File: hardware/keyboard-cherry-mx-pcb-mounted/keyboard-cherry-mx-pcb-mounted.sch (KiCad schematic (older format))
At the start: 1 part

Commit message: Adds general layout for the custom keyboard.
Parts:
- gave numbers to parts that had none: 1
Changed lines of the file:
@@
 $EndSheet
 $Comp
-L Sij_MCU:BGM13S U?
+L Sij_MCU:BGM13S U1
 U 1 1 5E85FADA
 P 6000 4000
-F 0 "U?" H 6000 4100 50  0000 C CNN
+F 0 "U1" H 6000 4100 50  0000 C CNN
 F 1 "BGM13S" H 6000 4000 50  0000 C CNN
 F 2 "Sij_MCU:BGM13S" H 6000 4150 50  0001 C CNN
@@
 	5600 5500 5700 5500
 $Comp
-L power:GND #PWR?
+L power:GND #PWR0101
 U 1 1 5E864ACF
 P 6000 5600
-F 0 "#PWR?" H 6000 5350 50  0001 C CNN
+F 0 "#PWR0101" H 6000 5350 50  0001 C CNN
 F 1 "GND" H 6005 5427 50  0000 C CNN
 F 2 "" H 6000 5600 50  0001 C CNN
@@
 SWO
 $Comp
-L power:GND #PWR?
+L power:GND #PWR0102
 U 1 1 5E873C21
 P 4650 3000
-F 0 "#PWR?" H 4650 2750 50  0001 C CNN
+F 0 "#PWR0102" H 4650 2750 50  0001 C CNN
 F 1 "GND" V 4655 2872 50  0000 R CNN
 F 2 "" H 4650 3000 50  0001 C CNN
@@
 	5100 2800 5200 2800
 $Comp
-L power:+3.3V #PWR?
+L power:+3.3V #PWR0103
 U 1 1 5E87759E
 P 6000 2200
-F 0 "#PWR?" H 6000 2050 50  0001 C CNN
+F 0 "#PWR0103" H 6000 2050 50  0001 C CNN
 F 1 "+3.3V" H 6015 2373 50  0000 C CNN
 F 2 "" H 6000 2200 50  0001 C CNN

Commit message: Adds STM32F413 to cherry mx pcb mounted board.
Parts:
- removed U1: BGM13S, Sij_MCU:BGM13S, symbol Sij_MCU:BGM13S
- added C? (x2): 4.7u, Capacitor_SMD:C_0805_2012Metric, symbol Device:C_Small
- added C? (x2): 15pF, Capacitor_SMD:C_0805_2012Metric, symbol Device:C_Small
- added C? (x4): 0.1u, Capacitor_SMD:C_0805_2012Metric, symbol Device:C_Small
- added C?: 1u, Capacitor_SMD:C_0805_2012Metric, symbol Device:C_Small
- added JP?: BootJumper, Jumper:SolderJumper-3_P1.3mm_Bridged12_Pad1.0x1.5mm, symbol Jumper:SolderJumper_3_Bridged12
- added SW?: RST, Button_Switch_SMD:SW_SPST_B3U-1000P, symbol Switch:SW_Push
- added U?: STM32F413CHUx, Package_DFN_QFN:QFN-48-1EP_7x7mm_P0.5mm_EP5.6x5.6mm, symbol MCU_ST_STM32F4:STM32F413CHUx
- added Y?: 8MHz, Crystal:Crystal_SMD_TXC_7A-2Pin_5x3.2mm, symbol Device:Crystal_Small
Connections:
- net labels added: D+, D-, OSC_IN, OSC_OUT, VBUS_SENSE, VCAP, ~NRST
- net labels removed: C15, SWO
- wire segments 56 -> 93
- no-connect marks 1 -> 0
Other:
- note added: "Reset Button"
- note added: "VDD Bypass Capacitors"
- note added: "VDDA Bypass Capacitors"

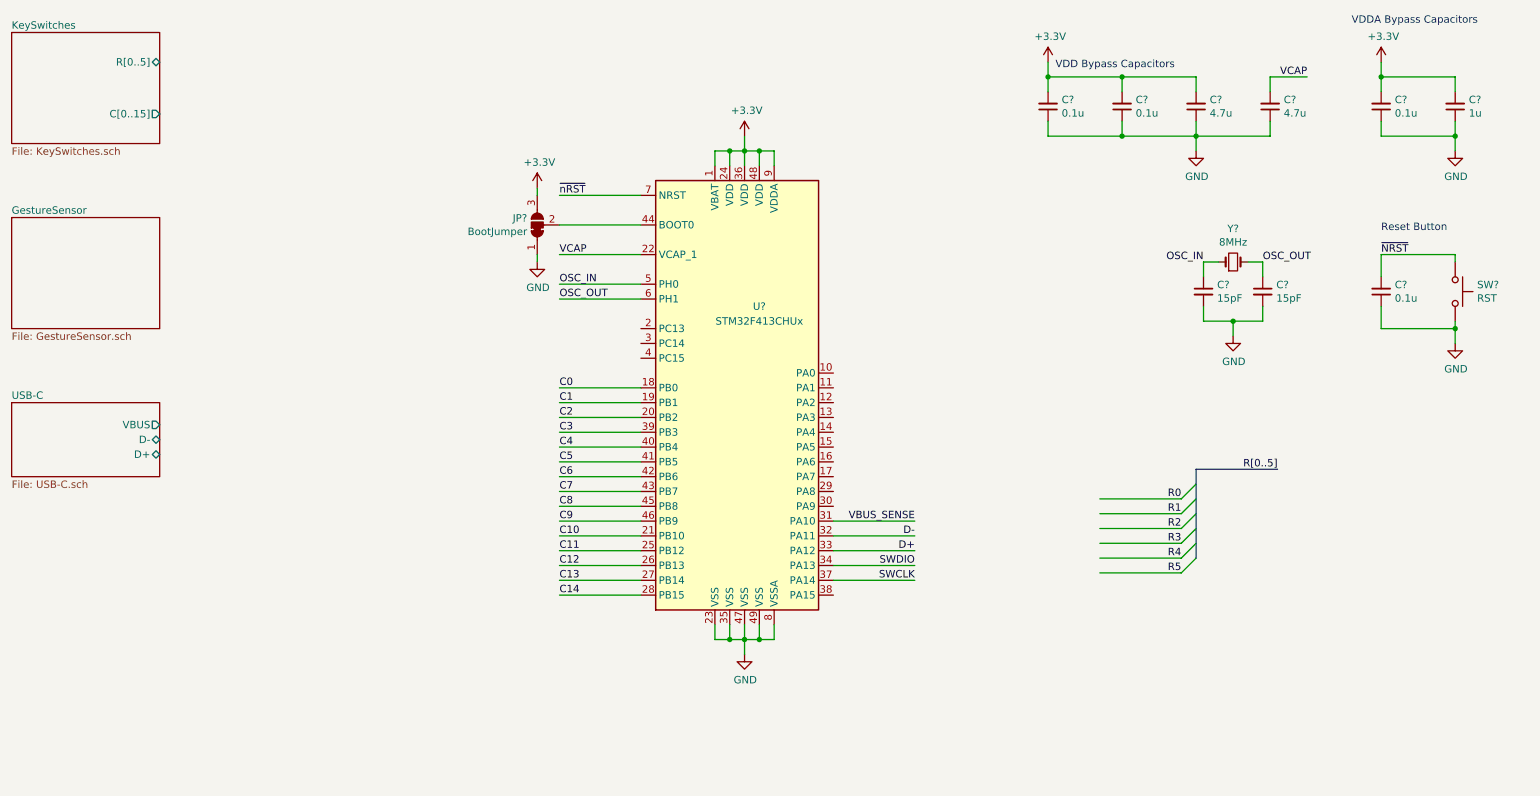
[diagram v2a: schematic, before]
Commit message: Adds gesture sensor interface. May change to bigger stm32 package.
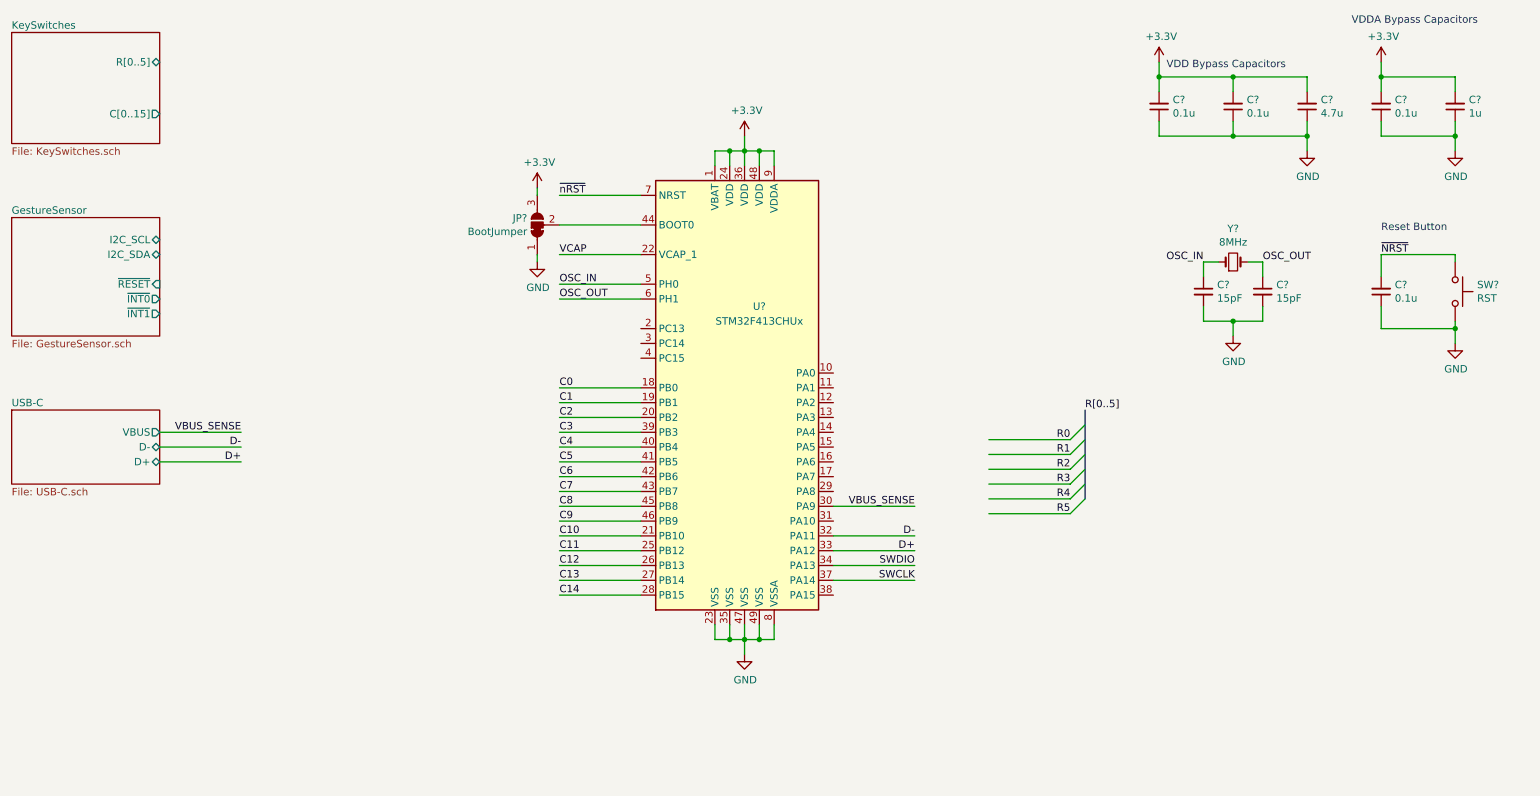
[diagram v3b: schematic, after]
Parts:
- removed C?: 4.7u, Capacitor_SMD:C_0805_2012Metric, symbol Device:C_Small
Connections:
- wire segments 93 -> 92
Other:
- moved on the sheet: C?
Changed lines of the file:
@@
 $EndComp
 $Sheet
-S 1000 2250 1000 750
+S 1000 2250 1000 800
 U 5E8711BD
 F0 "GestureSensor" 50
 F1 "GestureSensor.sch" 50
+F2 "I2C_SCL" B R 2000 2400 50
+F3 "I2C_SDA" B R 2000 2500 50
+F4 "~RESET" I R 2000 2700 50
+F5 "~INT0" O R 2000 2800 50
+F6 "~INT1" O R 2000 2900 50
 $EndSheet
 Wire Wire Line
@@
 ~nRST
 Wire Wire Line
-	8350 4150 8900 4150
-Wire Wire Line
-	8900 4250 8350 4250
-Wire Wire Line
-	8350 4350 8900 4350
-Wire Wire Line
-	8350 4450 8900 4450
-Text Label 8900 4150 2    50   ~ 0
+	7600 3750 8150 3750
+Wire Wire Line
+	8150 3850 7600 3850
+Wire Wire Line
+	7600 3950 8150 3950
+Wire Wire Line
+	7600 4050 8150 4050
+Text Label 8150 3750 2    50   ~ 0
 R0
-Text Label 8900 4250 2    50   ~ 0
+Text Label 8150 3850 2    50   ~ 0
 R1
-Text Label 8900 4350 2    50   ~ 0
+Text Label 8150 3950 2    50   ~ 0
 R2
-Text Label 8900 4450 2    50   ~ 0
+Text Label 8150 4050 2    50   ~ 0
 R3
 Wire Wire Line
-	8350 4550 8900 4550
-Wire Wire Line
-	8900 4650 8350 4650
-Text Label 8900 4550 2    50   ~ 0
+	7600 4150 8150 4150
+Wire Wire Line
+	8150 4250 7600 4250
+Text Label 8150 4150 2    50   ~ 0
 R4
-Text Label 8900 4650 2    50   ~ 0
+Text Label 8150 4250 2    50   ~ 0
 R5
 Entry Wire Line
-	9000 4550 8900 4650
+	8250 4150 8150 4250
 Entry Wire Line
-	9000 4450 8900 4550
+	8250 4050 8150 4150
 Entry Wire Line
-	9000 4350 8900 4450
+	8250 3950 8150 4050
 Entry Wire Line
-	9000 4250 8900 4350
+	8250 3850 8150 3950
 Entry Wire Line
-	9000 4150 8900 4250
+	8250 3750 8150 3850
 Entry Wire Line
-	9000 4050 8900 4150
-Wire Bus Line
-	9000 3950 9550 3950
-Text Label 9550 3950 2    50   ~ 0
+	8250 3650 8150 3750
+Text Label 8250 3550 0    50   ~ 0
 R[0..5]
 Wire Wire Line
@@
 	5850 1800 5950 1800
 $Comp
-L Device:C_Small C?
-U 1 1 5E71757F
-P 9500 1500
-F 0 "C?" H 9408 1454 50  0000 R CNN
-F 1 "4.7u" H 9408 1545 50  0000 R CNN
-F 2 "Capacitor_SMD:C_0805_2012Metric" H 9500 1500 50  0001 C CNN
-F 3 "~" H 9500 1500 50  0001 C CNN
-	1    9500 1500
-	-1   0    0    1
-$EndComp
-$Comp
 L Jumper:SolderJumper_3_Bridged12 JP?
 U 1 1 5E719EA9
@@
 L Device:C_Small C?
 U 1 1 5E73F523
-P 8000 1500
-F 0 "C?" H 7908 1454 50  0000 R CNN
-F 1 "0.1u" H 7908 1545 50  0000 R CNN
-F 2 "Capacitor_SMD:C_0805_2012Metric" H 8000 1500 50  0001 C CNN
-F 3 "~" H 8000 1500 50  0001 C CNN
-	1    8000 1500
+P 8750 1500
+F 0 "C?" H 8658 1454 50  0000 R CNN
+F 1 "0.1u" H 8658 1545 50  0000 R CNN
+F 2 "Capacitor_SMD:C_0805_2012Metric" H 8750 1500 50  0001 C CNN
+F 3 "~" H 8750 1500 50  0001 C CNN
+	1    8750 1500
 	-1   0    0    1
 $EndComp
@@
 L Device:C_Small C?
 U 1 1 5E73FD52
-P 8500 1500
-F 0 "C?" H 8408 1454 50  0000 R CNN
-F 1 "0.1u" H 8408 1545 50  0000 R CNN
-F 2 "Capacitor_SMD:C_0805_2012Metric" H 8500 1500 50  0001 C CNN
-F 3 "~" H 8500 1500 50  0001 C CNN
-	1    8500 1500
+P 9250 1500
+F 0 "C?" H 9158 1454 50  0000 R CNN
+F 1 "0.1u" H 9158 1545 50  0000 R CNN
+F 2 "Capacitor_SMD:C_0805_2012Metric" H 9250 1500 50  0001 C CNN
+F 3 "~" H 9250 1500 50  0001 C CNN
+	1    9250 1500
 	-1   0    0    1
 $EndComp
@@
 L Device:C_Small C?
 U 1 1 5E73FF6A
-P 9000 1500
-F 0 "C?" H 8908 1454 50  0000 R CNN
-F 1 "4.7u" H 8908 1545 50  0000 R CNN
-F 2 "Capacitor_SMD:C_0805_2012Metric" H 9000 1500 50  0001 C CNN
-F 3 "~" H 9000 1500 50  0001 C CNN
-	1    9000 1500
+P 9750 1500
+F 0 "C?" H 9658 1454 50  0000 R CNN
+F 1 "4.7u" H 9658 1545 50  0000 R CNN
+F 2 "Capacitor_SMD:C_0805_2012Metric" H 9750 1500 50  0001 C CNN
+F 3 "~" H 9750 1500 50  0001 C CNN
+	1    9750 1500
 	-1   0    0    1
 $EndComp
@@
 L power:+3.3V #PWR?
 U 1 1 5E743BF3
-P 8000 1200
-F 0 "#PWR?" H 8000 1050 50  0001 C CNN
-F 1 "+3.3V" H 8015 1373 50  0000 C CNN
-F 2 "" H 8000 1200 50  0001 C CNN
-F 3 "" H 8000 1200 50  0001 C CNN
-	1    8000 1200
-	1    0    0    -1
-$EndComp
-Wire Wire Line
-	9000 1300 9000 1400
-Wire Wire Line
-	8500 1400 8500 1300
-Connection ~ 8500 1300
-Wire Wire Line
-	8500 1300 9000 1300
-Wire Wire Line
-	8000 1400 8000 1300
-Wire Wire Line
-	8000 1300 8500 1300
+P 8750 1200
+F 0 "#PWR?" H 8750 1050 50  0001 C CNN
+F 1 "+3.3V" H 8765 1373 50  0000 C CNN
+F 2 "" H 8750 1200 50  0001 C CNN
+F 3 "" H 8750 1200 50  0001 C CNN
+	1    8750 1200
+	1    0    0    -1
+$EndComp
+Wire Wire Line
+	9750 1300 9750 1400
+Wire Wire Line
+	9250 1400 9250 1300
+Connection ~ 9250 1300
+Wire Wire Line
+	9250 1300 9750 1300
+Wire Wire Line
+	8750 1400 8750 1300
+Wire Wire Line
+	8750 1300 9250 1300
 $Comp
 L power:GND #PWR?
 U 1 1 5E748424
-P 9000 1800
-F 0 "#PWR?" H 9000 1550 50  0001 C CNN
-F 1 "GND" H 9005 1627 50  0000 C CNN
-F 2 "" H 9000 1800 50  0001 C CNN
-F 3 "" H 9000 1800 50  0001 C CNN
-	1    9000 1800
-	1    0    0    -1
-$EndComp
-Wire Wire Line
-	9000 1800 9000 1700
-Wire Wire Line
-	9000 1700 8500 1700
-Connection ~ 9000 1700
-Wire Wire Line
-	9000 1700 9000 1600
-Wire Wire Line
-	8000 1600 8000 1700
-Wire Wire Line
-	8500 1600 8500 1700
-Connection ~ 8500 1700
-Wire Wire Line
-	8500 1700 8000 1700
-Wire Wire Line
-	9500 1400 9500 1300
-Wire Wire Line
-	9500 1300 9750 1300
-Wire Wire Line
-	9500 1700 9500 1600
-Wire Wire Line
-	9500 1700 9000 1700
-Text Label 9750 1300 2    50   ~ 0
-VCAP
+P 9750 1800
+F 0 "#PWR?" H 9750 1550 50  0001 C CNN
+F 1 "GND" H 9755 1627 50  0000 C CNN
+F 2 "" H 9750 1800 50  0001 C CNN
+F 3 "" H 9750 1800 50  0001 C CNN
+	1    9750 1800
+	1    0    0    -1
+$EndComp
+Wire Wire Line
+	9750 1800 9750 1700
+Wire Wire Line
+	9750 1700 9250 1700
+Connection ~ 9750 1700
+Wire Wire Line
+	9750 1700 9750 1600
+Wire Wire Line
+	8750 1600 8750 1700
+Wire Wire Line
+	9250 1600 9250 1700
+Connection ~ 9250 1700
+Wire Wire Line
+	9250 1700 8750 1700
 $Comp
 L Device:C_Small C?
@@
 Text Notes 10050 950  0    50   ~ 0
 VDDA Bypass Capacitors
-Text Notes 8050 1250 0    50   ~ 0
+Text Notes 8800 1250 0    50   ~ 0
 VDD Bypass Capacitors
 $Comp
@@
 OSC_OUT
 $Sheet
-S 1000 3500 1000 500
+S 1000 3550 1000 500
 U 5E7D269A
 F0 "USB-C" 50
 F1 "USB-C.sch" 50
-F2 "D-" B R 2000 3750 50
-F3 "D+" B R 2000 3850 50
-F4 "VBUS" O R 2000 3650 50
+F2 "D-" B R 2000 3800 50
+F3 "D+" B R 2000 3900 50
+F4 "VBUS" O R 2000 3700 50
 $EndSheet
 Wire Wire Line
-	8000 1200 8000 1300
-Connection ~ 8000 1300
+	8750 1200 8750 1300
+Connection ~ 8750 1300
 Wire Wire Line
 	6550 4500 7100 4500
@@
 D+
 Wire Wire Line
-	6550 4300 7100 4300
+	6550 4200 7100 4200
+Text Label 7100 4200 2    50   ~ 0
+VBUS_SENSE
+Wire Wire Line
+	2000 3900 2550 3900
+Wire Wire Line
+	2000 3800 2550 3800
+Text Label 2550 3800 2    50   ~ 0
+D-
+Text Label 2550 3900 2    50   ~ 0
+D+
+Wire Wire Line
+	2000 3700 2550 3700
+Text Label 2550 3700 2    50   ~ 0
+VBUS_SENSE
 Wire Bus Line
-	9000 3950 9000 4550
-Text Label 7100 4300 2    50   ~ 0
-VBUS_SENSE
+	8250 3550 8250 4150
 $EndSCHEMATC

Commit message: Adds completed sensor and power connections. Still need to add USB footprint then sch are done for version 1.0
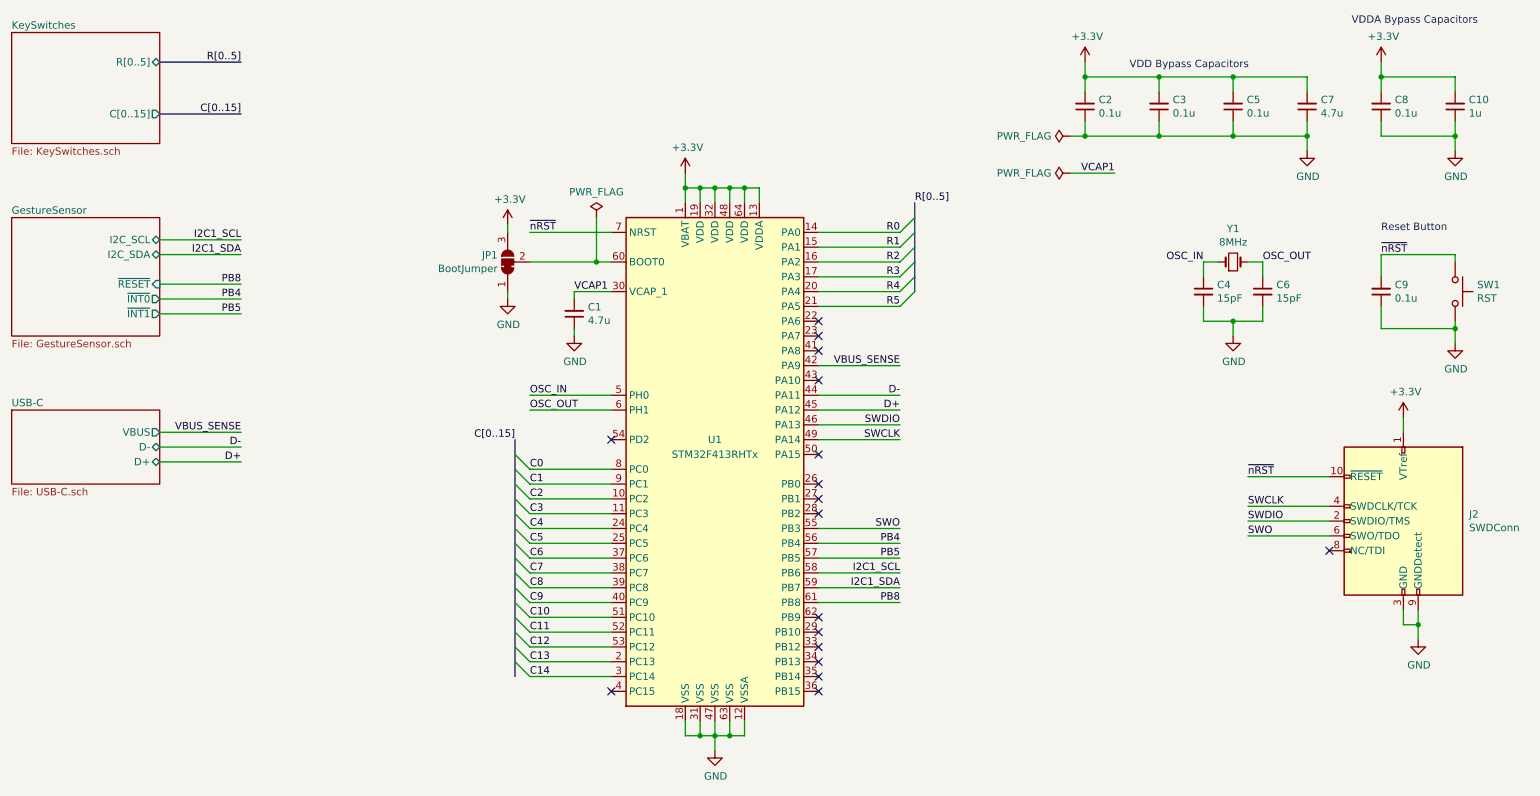
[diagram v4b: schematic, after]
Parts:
- removed JP?: BootJumper, Jumper:SolderJumper-3_P1.3mm_Bridged12_Pad1.0x1.5mm, symbol Jumper:SolderJumper_3_Bridged12
- removed U?: STM32F413CHUx, Package_DFN_QFN:QFN-48-1EP_7x7mm_P0.5mm_EP5.6x5.6mm, symbol MCU_ST_STM32F4:STM32F413CHUx
- added C1: 4.7u, Capacitor_SMD:C_0805_2012Metric, symbol Device:C_Small
- added C2: 0.1u, Capacitor_SMD:C_0805_2012Metric, symbol Device:C_Small
- added J2: SWDConn, Connector:Tag-Connect_TC2050-IDC-NL_2x05_P1.27mm_Vertical, symbol Connector:Conn_ARM_JTAG_SWD_10
- added JP1: BootJumper, Jumper:SolderJumper-3_P1.3mm_Bridged12_Pad1.0x1.5mm, symbol Jumper:SolderJumper_3_Bridged12
- added U1: STM32F413RHTx, Package_QFP:LQFP-64_10x10mm_P0.5mm, symbol MCU_ST_STM32F4:STM32F413RHTx
- gave numbers to parts that had none: 10
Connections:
- net labels added: C[0..15], I2C1_SCL, I2C1_SDA, PB4, PB5, PB8, SWO, VCAP1
- net labels removed: VCAP, ~NRST
- wire segments 92 -> 124
- no-connect marks 0 -> 17

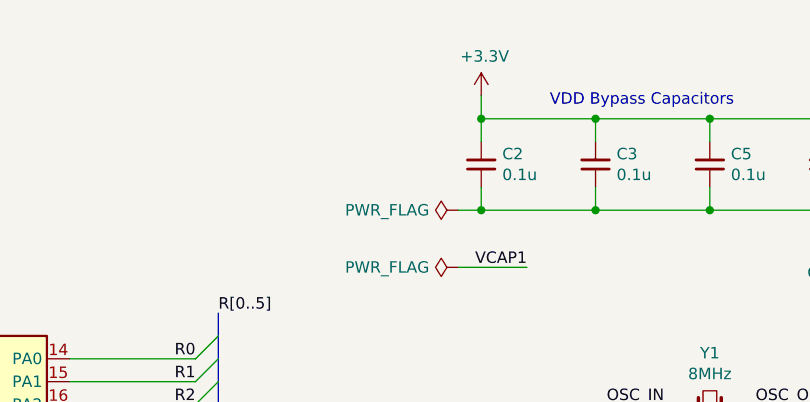
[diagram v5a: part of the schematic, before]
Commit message: Adds final key caps layout of a 75 keyboard.
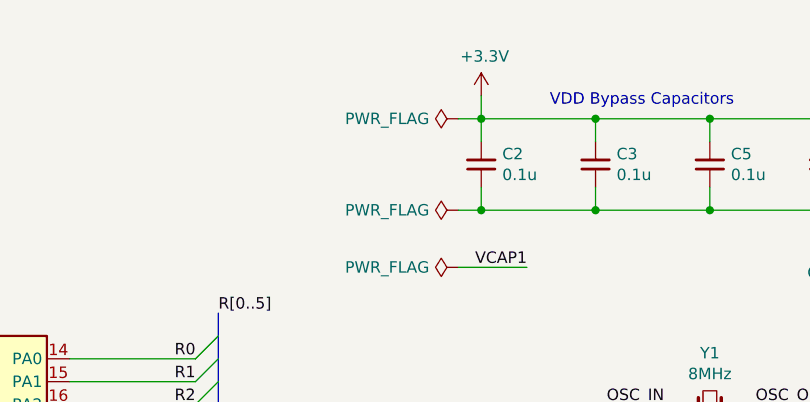
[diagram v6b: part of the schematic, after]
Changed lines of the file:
@@
 Wire Wire Line
 	4950 2550 4500 2550
+$Comp
+L power:PWR_FLAG #FLG0104
+U 1 1 5E7192AF
+P 8150 1300
+F 0 "#FLG0104" H 8150 1375 50  0001 C CNN
+F 1 "PWR_FLAG" V 8150 1427 50  0000 L CNN
+F 2 "" H 8150 1300 50  0001 C CNN
+F 3 "~" H 8150 1300 50  0001 C CNN
+	1    8150 1300
+	0    -1   -1   0
+$EndComp
+Wire Wire Line
+	8150 1300 8250 1300
 Wire Bus Line
 	7100 2150 7100 2750
